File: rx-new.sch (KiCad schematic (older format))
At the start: 18 parts

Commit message: Added some text
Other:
- note added: "Frederic is the best!!!11"
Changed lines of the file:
@@
 EESchema Schematic File Version 4
-LIBS:rx-new-cache
-EELAYER 29 0
+EELAYER 30 0
 EELAYER END
 $Descr A4 11693 8268
@@
 Wire Wire Line
 	6200 6200 6750 6200
+Text Notes 2600 4150 0    50   ~ 0
+Frederic is the best!!!11
 $EndSCHEMATC

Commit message: created_basic_idea
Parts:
- removed C?: 47u, symbol Device:CP_Small
- removed C?: 1u, symbol Device:CP_Small
- added C?: 1u, symbol Device:CP_Small
- added C? (x4): 47u, symbol Device:CP_Small
- added C? (x4): 1n, symbol Device:C_Small
- added C? (x3): 0.1u, symbol Device:C_Small
- added D? (x2): BAT42, Diode_THT:D_DO-35_SOD27_P7.62mm_Horizontal, symbol Diode:BAT42
- added Q?: BC858, Package_TO_SOT_SMD:SOT-23, symbol Transistor_BJT:BC858
- added R? (x4): 100k, symbol Device:R_Small_US
- added R?: 10k, symbol Device:R_Small_US
- added R?: 100E, symbol Device:R_Small_US
- R? (x2): value 2.2K -> 10k
- U?: value TPS79133-EP -> TPS791
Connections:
- net labels added: +12V, +Vf, -Vf, 4LO
- net labels removed: +3.3V, +5V
- wire segments 77 -> 89
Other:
- note added: "-Vf = 4V - 3.6V/2"
- note added: "Every supply C should be a tripple, high value (47µF, mid 0.1µf, small 1nF)"
- note added: "Need to be RF diodes for protection"
- note added: "Need to supply this with +Vf and -Vf\nmight also need 74LVX00 as a shaping buffer"
- note added: "Still need to define all resistor values to generate +Vf and -Vf"
- note added: "TPS791 handles higher input voltages\nNeed to add FB pin\n+Vf = 4V + 3.6V/2"
- note removed: "Frederic is the best!!!11"
- moved on the sheet: C?, R?, TR?, U?

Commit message: Added TPS79101 to custom library
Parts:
- removed U?: TPS791, Package_TO_SOT_SMD:SOT-23-5, symbol Regulator_Linear:TPS79333-EP
- added U?: TPS79101DBVREP, Texas_Instruments-TPS79101DBVREP-*, symbol custom_library:TPS79101DBVREP
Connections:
- net labels added: CLK_0
- net labels removed: CLK_2, RF_IN_N, RF_IN_P
- wire segments 89 -> 88
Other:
- moved on the sheet: C?, D?, R?, TR?

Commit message: power_supplies
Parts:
- added C?: 1n0, symbol Device:C_Small
- added C? (x2): 1n, symbol Device:C_Small
- added C?: 0.1u, symbol Device:C_Small
- added C?: 47u, symbol Device:CP_Small
- added Q?: BC848, Package_TO_SOT_SMD:SOT-23, symbol Transistor_BJT:BC848
- added R?: 1E, symbol Device:R_Small_US
- added R? (x2): 100k, symbol Device:R_Small_US
- R?: value 100E -> 1E
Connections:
- net -Vf is gone; now on net GND: C?.1, C?.1, C?.1, C?.1, C?.1, C?.2, C?.2, C?.2, C?.2, R?.1, R?.2, U?.8 (GND)
- net +12V: now also Q?.3 (C)
- net +Vf: now also R?.1; no longer U?.6 (~CLR), U?.6 (~CLR), U?.7 (~PRE), U?.7 (~PRE)
- net GND: now also C?.1, C?.1, C?.1, C?.1, C?.2, C?.2, C?.2, R?.2
- net VCC: now also U?.6 (~CLR), U?.6 (~CLR), U?.7 (~PRE), U?.7 (~PRE), C?.1, C?.2, C?.2, R?.2
- new net: Q?.1 (B), R?.1, R?.2
- new net: Q?.2 (E), R?.1
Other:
- note added: "+Vf = 4V + 2.5V"
- note added: "-Vf = 4V - 2.5V"
- note added: "need 74LVX00 as a shaping buffer"
- note removed: "-Vf = 4V - 3.6V/2"
- note removed: "Need to supply this with +Vf and -Vf\nmight also need 74LVX00 as a shaping buffer"
- note removed: "TPS791 handles higher input voltages\nNeed to add FB pin\n+Vf = 4V + 3.6V/2"
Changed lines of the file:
@@
 EESchema Schematic File Version 4
-EELAYER 30 0
+LIBS:rx-new-cache
+EELAYER 29 0
 EELAYER END
 $Descr A4 11693 8268
@@
 	3950 1450 4050 1450
 Connection ~ 3950 1450
-Text GLabel 3950 950  1    50   Input ~ 0
+Text GLabel 3950 1050 1    50   Input ~ 0
 +Vf
 Wire Wire Line
@@
 Text GLabel 3050 5300 2    50   Output ~ 0
 +Vf
-Text Notes 2400 4850 0    50   ~ 0
+Text Notes 3850 4350 0    50   ~ 0
 Power section
 $Comp
@@
 Text GLabel 3000 3550 2    50   Output ~ 0
 CLK_1
-Wire Wire Line
-	3950 3050 4050 3050
 Text GLabel 3950 3150 3    50   Input ~ 0
 -Vf
 Wire Wire Line
-	3950 2850 3950 3050
-Connection ~ 3950 3050
-Wire Wire Line
-	3950 3050 3950 3150
+	3950 2850 3950 2900
 $Comp
 L Device:R_Small_US R?
@@
 Connection ~ 2250 5500
 Text Notes 700  6350 0    50   ~ 0
-TPS791 handles higher input voltages\nNeed to add FB pin\n+Vf = 4V + 3.6V/2
++Vf = 4V + 2.5V
 Text GLabel 3800 6350 3    50   Input ~ 0
 -Vf
@@
 P 2150 6750
 F 0 "R?" V 1945 6750 50  0000 C CNN
-F 1 "100E" V 2036 6750 50  0000 C CNN
+F 1 "1E" V 2036 6750 50  0000 C CNN
 F 2 "" H 2150 6750 50  0001 C CNN
 F 3 "~" H 2150 6750 50  0001 C CNN
@@
 Connection ~ 1550 6950
 Text Notes 1200 7400 0    50   ~ 0
--Vf = 4V - 3.6V/2
+-Vf = 4V - 2.5V
 Text Notes 800  7700 0    50   ~ 0
 Still need to define all resistor values to generate +Vf and -Vf
@@
 Text GLabel 2400 3550 0    50   Input ~ 0
 4LO
-Text GLabel 1800 3200 1    50   Input ~ 0
-+Vf
-Text GLabel 2650 3200 1    50   Input ~ 0
-+Vf
-Text GLabel 1800 3700 3    50   Input ~ 0
-+Vf
-Text GLabel 2650 3700 3    50   Input ~ 0
-+Vf
 Text Notes 1350 4050 0    50   ~ 0
-Need to supply this with +Vf and -Vf\nmight also need 74LVX00 as a shaping buffer
+need 74LVX00 as a shaping buffer
 $Comp
 L power:GND #PWR?
@@
 Text GLabel 4250 1250 2    50   Input ~ 0
 -Vf
-Wire Wire Line
-	3950 950  3950 1050
-Connection ~ 3950 1050
 Wire Wire Line
 	3950 1050 3950 1250
@@
 Wire Wire Line
 	3500 1950 3550 1950
+Text GLabel 1650 3300 1    50   Input ~ 0
++Vd
+Text GLabel 1650 3600 3    50   Input ~ 0
+-Vf
+$Comp
+L Device:C_Small C?
+U 1 1 5F6F2D37
+P 4150 3100
+F 0 "C?" V 4150 3500 50  0000 C CNN
+F 1 "1n0" V 4150 3700 50  0000 C CNN
+F 2 "" H 4150 3100 50  0001 C CNN
+F 3 "~" H 4150 3100 50  0001 C CNN
+	1    4150 3100
+	0    1    1    0
+$EndComp
+Text GLabel 4250 3100 2    50   Input ~ 0
+-Vf
+$Comp
+L Device:C_Small C?
+U 1 1 5F6F2D3E
+P 4150 2900
+F 0 "C?" V 4150 3300 50  0000 C CNN
+F 1 "1n" V 4150 3500 50  0000 C CNN
+F 2 "" H 4150 2900 50  0001 C CNN
+F 3 "~" H 4150 2900 50  0001 C CNN
+	1    4150 2900
+	0    1    1    0
+$EndComp
+Text GLabel 4250 2900 2    50   Input ~ 0
+-Vf
+Wire Wire Line
+	4050 2900 3950 2900
+Connection ~ 3950 2900
+Wire Wire Line
+	4050 3100 3950 3100
+Connection ~ 3950 3100
+Wire Wire Line
+	3950 3100 3950 3150
+Wire Wire Line
+	3950 2900 3950 3100
+Text GLabel 3050 4500 2    50   Output ~ 0
++Vd
+$Comp
+L Device:C_Small C?
+U 1 1 5F71038B
+P 2450 4700
+F 0 "C?" V 2450 5100 50  0000 C CNN
+F 1 "0.1u" V 2450 5300 50  0000 C CNN
+F 2 "" H 2450 4700 50  0001 C CNN
+F 3 "~" H 2450 4700 50  0001 C CNN
+	1    2450 4700
+	-1   0    0    1
+$EndComp
+$Comp
+L Device:CP_Small C?
+U 1 1 5F710395
+P 2850 4700
+F 0 "C?" V 2850 4250 50  0000 L CNN
+F 1 "47u" V 2850 4050 50  0000 L CNN
+F 2 "" H 2850 4700 50  0001 C CNN
+F 3 "~" H 2850 4700 50  0001 C CNN
+	1    2850 4700
+	1    0    0    -1
+$EndComp
+Wire Wire Line
+	2850 4600 2850 4500
+$Comp
+L Device:C_Small C?
+U 1 1 5F7103A0
+P 2650 4700
+F 0 "C?" V 2650 5100 50  0000 C CNN
+F 1 "1n" V 2650 5300 50  0000 C CNN
+F 2 "" H 2650 4700 50  0001 C CNN
+F 3 "~" H 2650 4700 50  0001 C CNN
+	1    2650 4700
+	-1   0    0    1
+$EndComp
+Wire Wire Line
+	2850 4500 3050 4500
+Connection ~ 2850 4500
+$Comp
+L power:GND #PWR?
+U 1 1 5F7103AC
+P 2450 4800
+F 0 "#PWR?" H 2450 4550 50  0001 C CNN
+F 1 "GND" H 2455 4627 50  0001 C CNN
+F 2 "" H 2450 4800 50  0001 C CNN
+F 3 "" H 2450 4800 50  0001 C CNN
+	1    2450 4800
+	1    0    0    -1
+$EndComp
+$Comp
+L power:GND #PWR?
+U 1 1 5F7103B6
+P 2650 4800
+F 0 "#PWR?" H 2650 4550 50  0001 C CNN
+F 1 "GND" H 2655 4627 50  0001 C CNN
+F 2 "" H 2650 4800 50  0001 C CNN
+F 3 "" H 2650 4800 50  0001 C CNN
+	1    2650 4800
+	1    0    0    -1
+$EndComp
+$Comp
+L power:GND #PWR?
+U 1 1 5F7103C0
+P 2850 4800
+F 0 "#PWR?" H 2850 4550 50  0001 C CNN
+F 1 "GND" H 2855 4627 50  0001 C CNN
+F 2 "" H 2850 4800 50  0001 C CNN
+F 3 "" H 2850 4800 50  0001 C CNN
+	1    2850 4800
+	1    0    0    -1
+$EndComp
+Wire Wire Line
+	2450 4500 2450 4600
+Wire Wire Line
+	2450 4500 2650 4500
+Wire Wire Line
+	2650 4500 2650 4600
+Connection ~ 2650 4500
+Wire Wire Line
+	2650 4500 2850 4500
+Text GLabel 1800 3200 1    50   Input ~ 0
++Vd
+Text GLabel 2650 3200 1    50   Input ~ 0
++Vd
+Text GLabel 1800 3700 3    50   Input ~ 0
++Vd
+Text GLabel 2650 3700 3    50   Input ~ 0
++Vd
+$Comp
+L Transistor_BJT:BC848 Q?
+U 1 1 5F72FAE9
+P 2050 4600
+F 0 "Q?" V 2378 4600 50  0000 C CNN
+F 1 "BC848" V 2287 4600 50  0000 C CNN
+F 2 "Package_TO_SOT_SMD:SOT-23" H 2250 4525 50  0001 L CIN
+F 3 "http://www.infineon.com/dgdl/Infineon-BC847SERIES_BC848SERIES_BC849SERIES_BC850SERIES-DS-v01_01-en.pdf?fileId=db3a304314dca389011541d4630a1657" H 2050 4600 50  0001 L CNN
+	1    2050 4600
+	0    -1   -1   0
+$EndComp
+$Comp
+L Device:R_Small_US R?
+U 1 1 5F733C03
+P 2350 4500
+F 0 "R?" V 2145 4500 50  0000 C CNN
+F 1 "1E" V 2236 4500 50  0000 C CNN
+F 2 "" H 2350 4500 50  0001 C CNN
+F 3 "~" H 2350 4500 50  0001 C CNN
+	1    2350 4500
+	0    -1   -1   0
+$EndComp
+Connection ~ 2450 4500
+Text GLabel 1850 4500 0    50   Input ~ 0
++12V
+$Comp
+L Device:R_Small_US R?
+U 1 1 5F740C78
+P 1950 4800
+F 0 "R?" V 1745 4800 50  0000 C CNN
+F 1 "100k" V 1836 4800 50  0000 C CNN
+F 2 "" H 1950 4800 50  0001 C CNN
+F 3 "~" H 1950 4800 50  0001 C CNN
+	1    1950 4800
+	0    -1   -1   0
+$EndComp
+$Comp
+L Device:R_Small_US R?
+U 1 1 5F740C82
+P 2150 4800
+F 0 "R?" V 1945 4800 50  0000 C CNN
+F 1 "100k" V 2036 4800 50  0000 C CNN
+F 2 "" H 2150 4800 50  0001 C CNN
+F 3 "~" H 2150 4800 50  0001 C CNN
+	1    2150 4800
+	0    -1   -1   0
+$EndComp
+$Comp
+L power:GND #PWR?
+U 1 1 5F740C8C
+P 2250 4800
+F 0 "#PWR?" H 2250 4550 50  0001 C CNN
+F 1 "GND" H 2255 4627 50  0001 C CNN
+F 2 "" H 2250 4800 50  0001 C CNN
+F 3 "" H 2250 4800 50  0001 C CNN
+	1    2250 4800
+	0    -1   -1   0
+$EndComp
+Connection ~ 2050 4800
+Text GLabel 1850 4800 0    50   Input ~ 0
++Vf
 $EndSCHEMATC

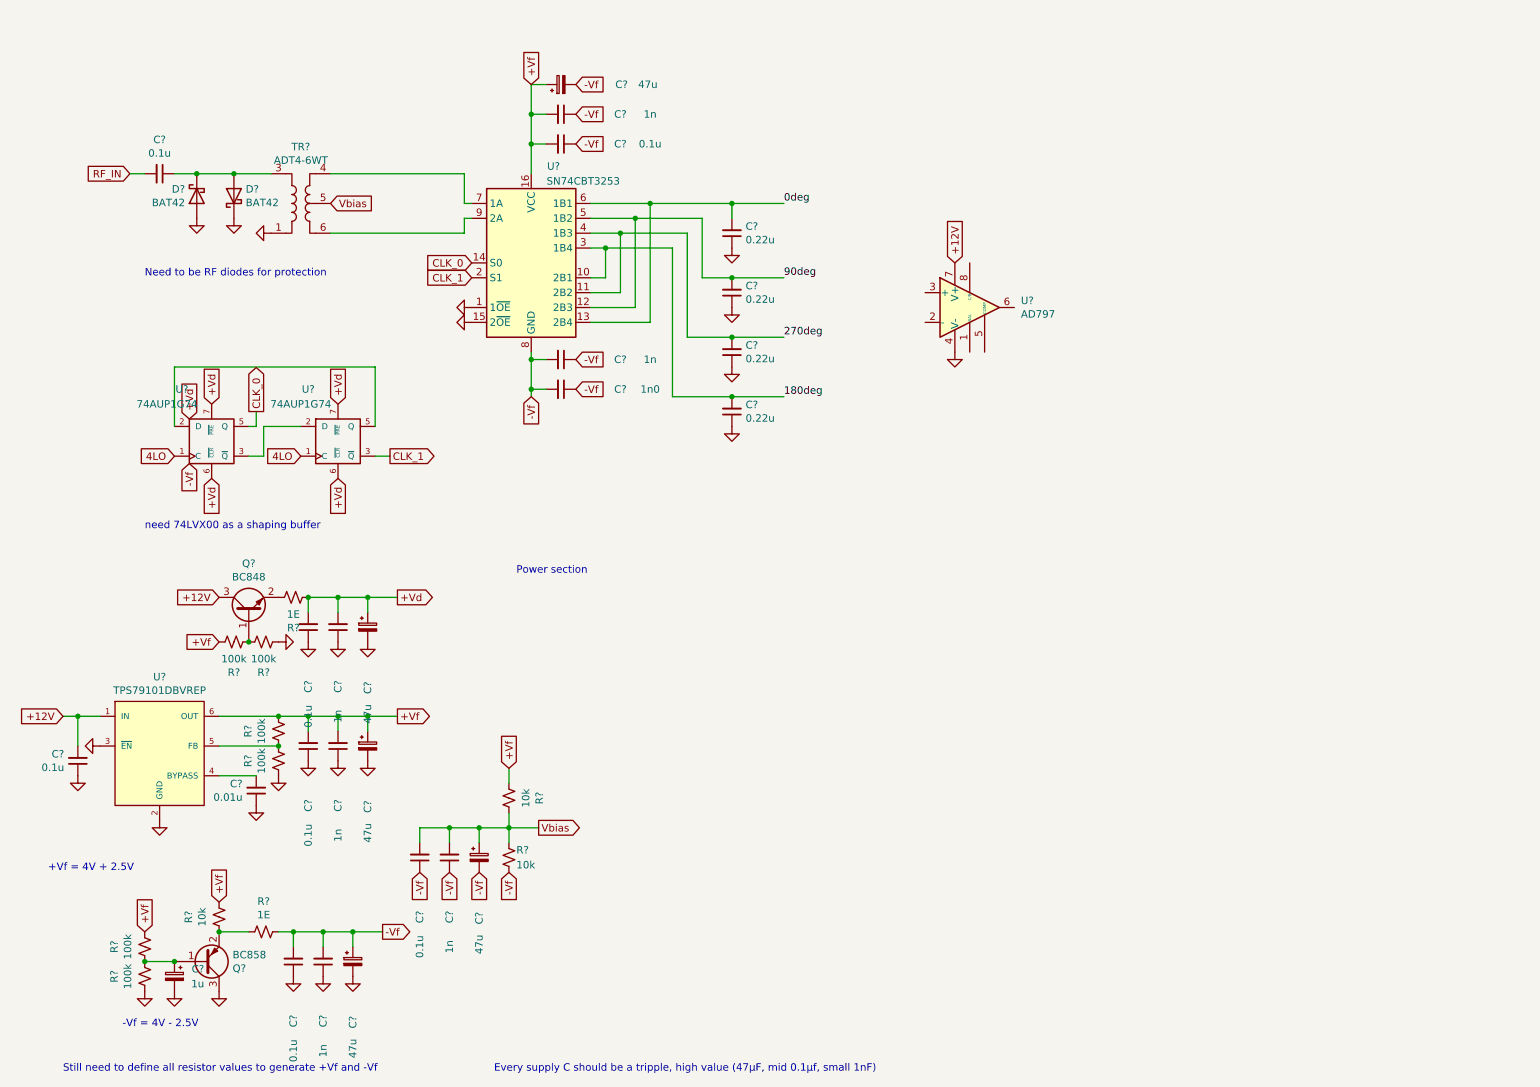
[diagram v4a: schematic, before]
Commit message: opamps_buffer_errors
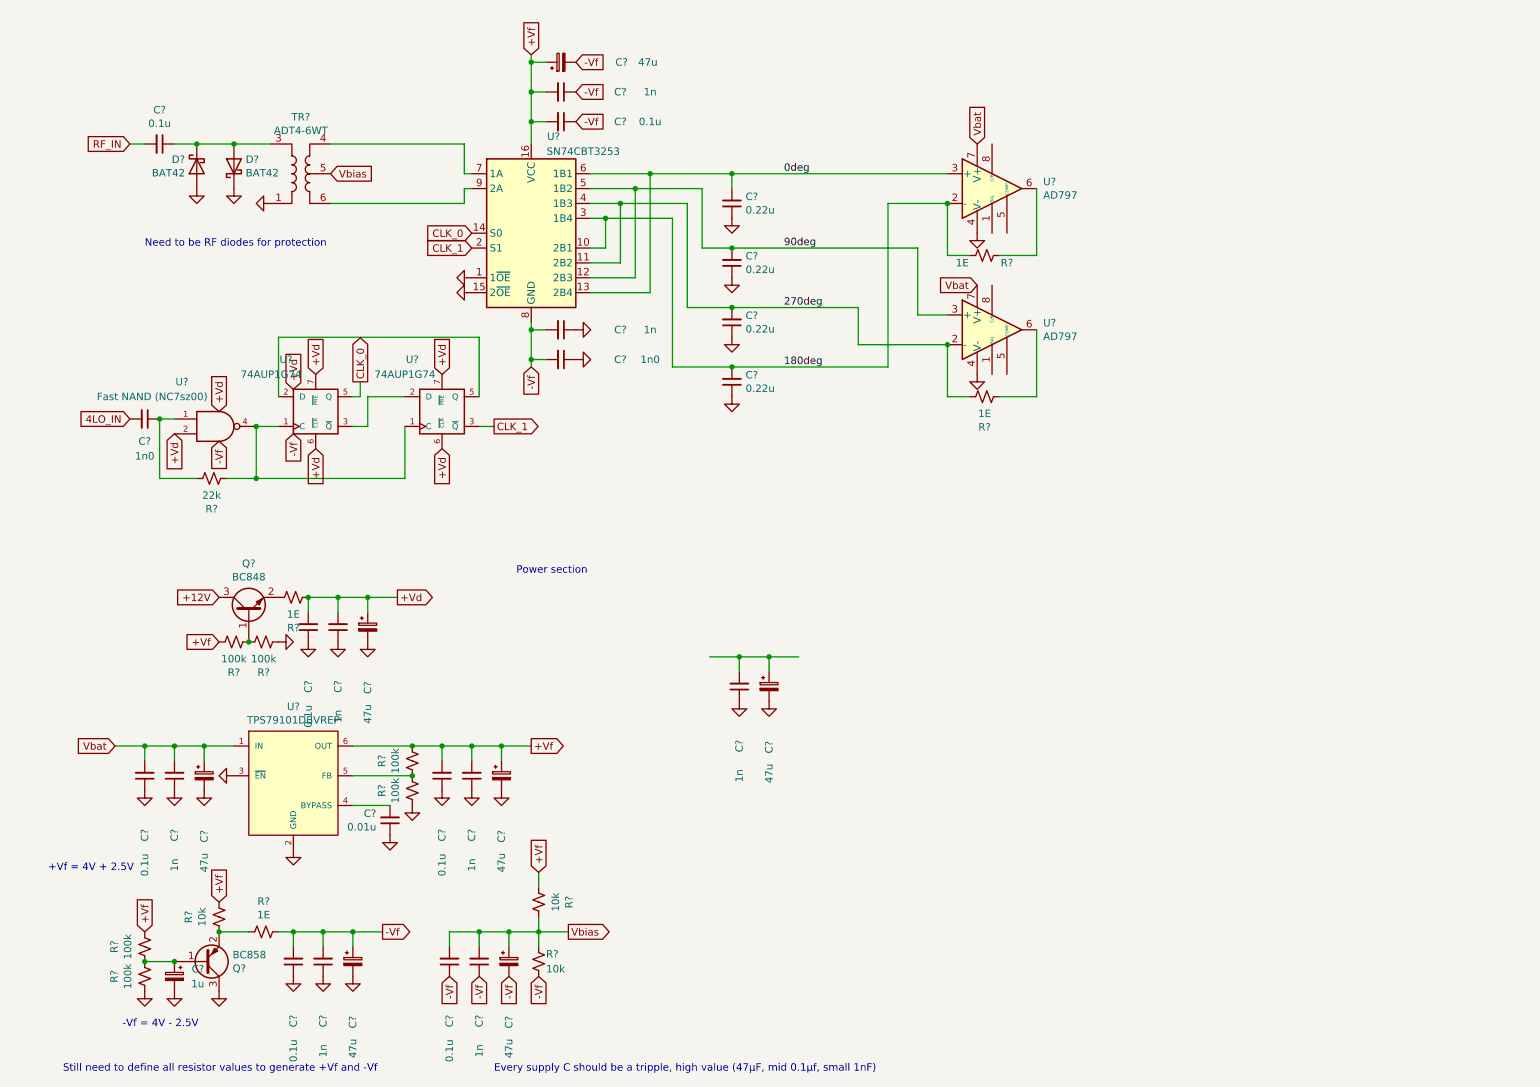
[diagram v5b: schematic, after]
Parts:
- removed C?: 0.1u, symbol Device:C_Small
- added C? (x2): 47u, symbol Device:CP_Small
- added C? (x2): 1n, symbol Device:C_Small
- added C?: 0.1u, symbol Device:C_Small
- added C?: 1n0, symbol Device:C_Small
- added R? (x2): 1E, symbol Device:R_Small_US
- added R?: 22k, symbol Device:R_Small_US
- added U?: AD797, symbol Amplifier_Operational:AD797
- added U?: Fast NAND (NC7sz00), symbol 74xGxx:74LVC1G00
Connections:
- net +12V: no longer U?.1 (IN), U?.7 (V+)
- net 0deg: now also U?.3 (+)
- net 180deg: now also U?.2 (-), R?.1
- net 270deg: now also R?.1, U?.2 (-)
- net 90deg: now also U?.3 (+)
- net GND: now also C?.1, C?.1, C?.1, C?.2, C?.2, U?.3 (GND), U?.4 (V-)
- net VCC: now also U?.2, U?.5 (VCC)
- net at U?.6: now also R?.2
- net 4LO: no longer names the net of U?.1 (C), U?.1 (C)
- net 4LO: now also R?.2, U?.4
- new net: C?.1, C?.2
- new net: R?.2, U?.6
- new net: C?.1, R?.1, U?.1
- new net 4LO_IN: C?.2
- new net Vbat: C?.1, C?.2, C?.2, U?.1 (IN), U?.7 (V+), U?.7 (V+)
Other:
- note removed: "need 74LVX00 as a shaping buffer"
- moved on the sheet: C?, D?, R?, TR?, U?
